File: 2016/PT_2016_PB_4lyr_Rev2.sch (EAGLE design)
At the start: 147 parts, among them M1+ ANDERSON_POWERPOLEPP45_PCB_HO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, M1- ANDERSON_POWERPOLEPP45_PCB_HO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, M2+ ANDERSON_POWERPOLEPP45_PCB_HO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, M2- ANDERSON_POWERPOLEPP45_PCB_HO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, M2-1 ANDERSON_POWERPOLEPP45_PCB_HO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, M2-2 ANDERSON_POWERPOLEPP45_PCB_HO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, M2-3 ANDERSON_POWERPOLEPP45_PCB_HO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, M2-4 ANDERSON_POWERPOLEPP45_PCB_HO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, M3+ ANDERSON_POWERPOLEPP45_PCB_HO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, M3- ANDERSON_POWERPOLEPP45_PCB_HO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, M4+ ANDERSON_POWERPOLEPP45_PCB_HO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, M4- ANDERSON_POWERPOLEPP45_PCB_HO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, M5+ ANDERSON_POWERPOLEPP45_PCB_HO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, M5- ANDERSON_POWERPOLEPP45_PCB_HO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, M6+ ANDERSON_POWERPOLEPP45_PCB_HO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, M6- ANDERSON_POWERPOLEPP45_PCB_HO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, Q1 Q_IRFS7437PbF, Q11 Q_IRFS7437PbF, Q12 2N7002, Q14 Q_IRFS7437PbF, Q16 Q_IRFS7437PbF, Q2 2N7002, Q20 Q_IRFS7437PbF, Q6 Q_IRFS7437PbF, Q7 Q_IRFS7437PbF, Q9 Q_IRFS7437PbF, X1 22-23-2041

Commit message: Added space for addition mounting wings and started moving components
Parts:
- removed M2-1, M2-2, M2-3, M2-4: ANDERSON_POWERPOLEPP45_PCB_HORIZ_RIGHT, MRDT-Connectors:ANDERSON_POWERPOLEPP45_PCB_HORIZ_RIGHT
- removed X1: 22-23-2041, con-molex:22-23-2041
- AUX1+, AUX2+, M1+, M2+, M3+, M4+, M5+, M6+: value ANDERSON_POWERPOLEPP45_PCB_HORIZ_RIGHT -> ANDERSON_POWERPOLEPP45_PCB_HORIZ_RIGHT_2HIGH; device MRDT-Connectors:ANDERSON_POWERPOLEPP45_PCB_HORIZ_RIGHT -> MRDT-Connectors:ANDERSON_POWERPOLEPP45_PCB_HORIZ_RIGHT_2HIGH
- C16, C24, C26, C28, C30, C32, C36, C7: value 10µF -> .1µF
- U$28, U$29: value ANDERSON_POWERPOLEPP45_PCB_HORIZ_RIGHT_2HIGH -> ANDERSON_POWERPOLEPP45_PCB_HORIZ_RIGHT; device MRDT-Connectors:ANDERSON_POWERPOLEPP45_PCB_HORIZ_RIGHT_2HIGH -> MRDT-Connectors:ANDERSON_POWERPOLEPP45_PCB_HORIZ_RIGHT
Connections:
- removed net N$11: M2-2.P$1, X1-1.S
- removed net N$3: M2-3.P$1, X1-4.S
- removed net N$5: M2-1.P$1, X1-3.S
- removed net N$8: M2-4.P$1, X1-2.S

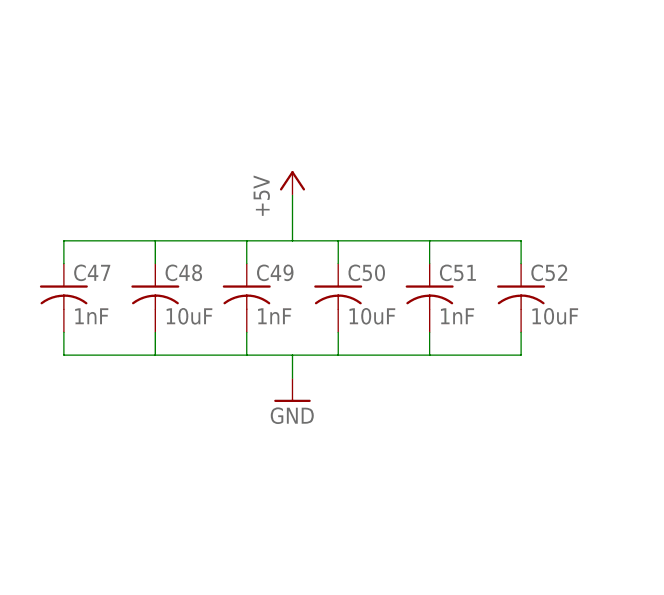
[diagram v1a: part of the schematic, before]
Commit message: Changed 5V Caps
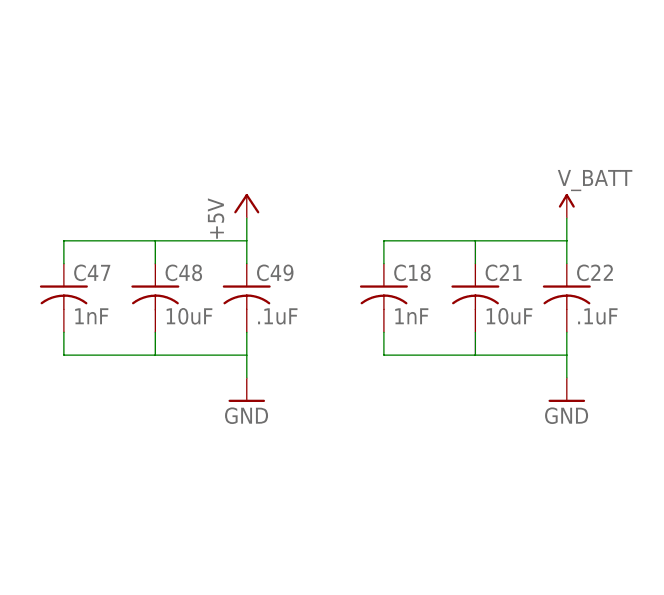
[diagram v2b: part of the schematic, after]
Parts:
- removed C50, C52: 10uF, resistor:C-USC1206
- removed C51: 1nF, resistor:C-USC1206
- added C18: 1nF, resistor:C-USC1206
- added C21: 10uF, resistor:C-USC1206
- added C22: .1uF, resistor:C-USC1206
- C49: value 1nF -> .1uF
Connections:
- net +5V: no longer C50.1, C51.1, C52.1
- net GND: now also C18.2, C21.2, C22.2; no longer C50.2, C51.2, C52.2
- net V_BATT: now also C18.1, C21.1, C22.1
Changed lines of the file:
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@@
 <part name="C47" library="resistor" deviceset="C-US" device="C1206" value="1nF"/>
 <part name="C48" library="resistor" deviceset="C-US" device="C1206" value="10uF"/>
-<part name="C49" library="resistor" deviceset="C-US" device="C1206" value="1nF"/>
-<part name="C50" library="resistor" deviceset="C-US" device="C1206" value="10uF"/>
-<part name="C51" library="resistor" deviceset="C-US" device="C1206" value="1nF"/>
-<part name="C52" library="resistor" deviceset="C-US" device="C1206" value="10uF"/>
+<part name="C49" library="resistor" deviceset="C-US" device="C1206" value=".1uF"/>
 <part name="P+25" library="supply1" deviceset="+5V" device=""/>
 <part name="GND95" library="SparkFun-Aesthetics" deviceset="GND" device=""/>
@@
 <part name="GND43" library="SparkFun-Aesthetics" deviceset="GND" device=""/>
 <part name="C17" library="resistor" deviceset="C-US" device="C1206" value="1nF"/>
+<part name="C18" library="resistor" deviceset="C-US" device="C1206" value="1nF"/>
+<part name="C21" library="resistor" deviceset="C-US" device="C1206" value="10uF"/>
+<part name="C22" library="resistor" deviceset="C-US" device="C1206" value=".1uF"/>
+<part name="GND45" library="SparkFun-Aesthetics" deviceset="GND" device=""/>
+<part name="SUPPLY16" library="SparkFun-Aesthetics" deviceset="V_BATT" device=""/>
 </parts>
 <sheets>
@@
 <instance part="GND94" gate="1" x="111.76" y="40.64"/>
 <instance part="C47" gate="G$1" x="195.58" y="5.08"/>
-<instance part="C48" gate="G$1" x="205.74" y="5.08"/>
-<instance part="C49" gate="G$1" x="215.9" y="5.08"/>
-<instance part="C50" gate="G$1" x="226.06" y="5.08"/>
-<instance part="C51" gate="G$1" x="236.22" y="5.08"/>
-<instance part="C52" gate="G$1" x="246.38" y="5.08"/>
-<instance part="P+25" gate="1" x="220.98" y="17.78"/>
-<instance part="GND95" gate="1" x="220.98" y="-7.62"/>
+<instance part="C48" gate="G$1" x="205.74" y="5.08" smashed="yes">
+<attribute name="NAME" x="206.756" y="5.715" size="1.778" layer="95"/>
+<attribute name="VALUE" x="206.756" y="0.889" size="1.778" layer="96"/>
+</instance>
+<instance part="C49" gate="G$1" x="215.9" y="5.08" smashed="yes">
+<attribute name="NAME" x="216.916" y="5.715" size="1.778" layer="95"/>
+<attribute name="VALUE" x="216.916" y="0.889" size="1.778" layer="96"/>
+</instance>
+<instance part="P+25" gate="1" x="215.9" y="15.24"/>
+<instance part="GND95" gate="1" x="215.9" y="-7.62"/>
 <instance part="SUPPLY2" gate="G$1" x="-518.16" y="231.14"/>
 <instance part="Q1" gate="G$1" x="-520.7" y="182.88"/>
@@
 <instance part="GND43" gate="1" x="73.66" y="114.3"/>
 <instance part="C17" gate="G$1" x="73.66" y="124.46"/>
+<instance part="C18" gate="G$1" x="231.14" y="5.08"/>
+<instance part="C21" gate="G$1" x="241.3" y="5.08" smashed="yes">
+<attribute name="NAME" x="242.316" y="5.715" size="1.778" layer="95"/>
+<attribute name="VALUE" x="242.316" y="0.889" size="1.778" layer="96"/>
+</instance>
+<instance part="C22" gate="G$1" x="251.46" y="5.08" smashed="yes">
+<attribute name="NAME" x="252.476" y="5.715" size="1.778" layer="95"/>
+<attribute name="VALUE" x="252.476" y="0.889" size="1.778" layer="96"/>
+</instance>
+<instance part="GND45" gate="1" x="251.46" y="-7.62"/>
+<instance part="SUPPLY16" gate="G$1" x="251.46" y="12.7"/>
 </instances>
 <busses>
@@
 <pinref part="C47" gate="G$1" pin="2"/>
 <wire x1="195.58" y1="0" x2="195.58" y2="-2.54" width="0.1524" layer="91"/>
-<pinref part="C52" gate="G$1" pin="2"/>
 <wire x1="195.58" y1="-2.54" x2="205.74" y2="-2.54" width="0.1524" layer="91"/>
-<wire x1="215.9" y1="-2.54" x2="220.98" y2="-2.54" width="0.1524" layer="91"/>
-<wire x1="220.98" y1="-2.54" x2="226.06" y2="-2.54" width="0.1524" layer="91"/>
-<wire x1="236.22" y1="-2.54" x2="246.38" y2="-2.54" width="0.1524" layer="91"/>
-<wire x1="246.38" y1="-2.54" x2="246.38" y2="0" width="0.1524" layer="91"/>
-<pinref part="C51" gate="G$1" pin="2"/>
-<wire x1="236.22" y1="0" x2="236.22" y2="-2.54" width="0.1524" layer="91"/>
-<pinref part="C50" gate="G$1" pin="2"/>
-<wire x1="236.22" y1="-2.54" x2="226.06" y2="-2.54" width="0.1524" layer="91"/>
-<wire x1="226.06" y1="-2.54" x2="226.06" y2="0" width="0.1524" layer="91"/>
 <pinref part="C49" gate="G$1" pin="2"/>
 <wire x1="215.9" y1="0" x2="215.9" y2="-2.54" width="0.1524" layer="91"/>
@@
 <wire x1="205.74" y1="-2.54" x2="205.74" y2="0" width="0.1524" layer="91"/>
 <pinref part="GND95" gate="1" pin="GND"/>
-<wire x1="220.98" y1="-5.08" x2="220.98" y2="-2.54" width="0.1524" layer="91"/>
+<wire x1="215.9" y1="-5.08" x2="215.9" y2="-2.54" width="0.1524" layer="91"/>
 </segment>
 <segment>
@@
 <pinref part="GND43" gate="1" pin="GND"/>
 <wire x1="73.66" y1="119.38" x2="73.66" y2="116.84" width="0.1524" layer="91"/>
+</segment>
+<segment>
+<pinref part="C18" gate="G$1" pin="2"/>
+<wire x1="231.14" y1="0" x2="231.14" y2="-2.54" width="0.1524" layer="91"/>
+<wire x1="231.14" y1="-2.54" x2="241.3" y2="-2.54" width="0.1524" layer="91"/>
+<pinref part="C22" gate="G$1" pin="2"/>
+<wire x1="251.46" y1="0" x2="251.46" y2="-2.54" width="0.1524" layer="91"/>
+<pinref part="C21" gate="G$1" pin="2"/>
+<wire x1="251.46" y1="-2.54" x2="241.3" y2="-2.54" width="0.1524" layer="91"/>
+<wire x1="241.3" y1="-2.54" x2="241.3" y2="0" width="0.1524" layer="91"/>
+<pinref part="GND45" gate="1" pin="GND"/>
+<wire x1="251.46" y1="-5.08" x2="251.46" y2="-2.54" width="0.1524" layer="91"/>
 </segment>
 </net>
@@
 <wire x1="-68.58" y1="-38.1" x2="-55.88" y2="-38.1" width="0.1524" layer="91"/>
 </segment>
+<segment>
+<pinref part="C18" gate="G$1" pin="1"/>
+<wire x1="231.14" y1="7.62" x2="231.14" y2="10.16" width="0.1524" layer="91"/>
+<wire x1="231.14" y1="10.16" x2="241.3" y2="10.16" width="0.1524" layer="91"/>
+<wire x1="251.46" y1="12.7" x2="251.46" y2="10.16" width="0.1524" layer="91"/>
+<pinref part="C22" gate="G$1" pin="1"/>
+<wire x1="251.46" y1="7.62" x2="251.46" y2="10.16" width="0.1524" layer="91"/>
+<pinref part="C21" gate="G$1" pin="1"/>
+<wire x1="251.46" y1="10.16" x2="241.3" y2="10.16" width="0.1524" layer="91"/>
+<wire x1="241.3" y1="10.16" x2="241.3" y2="7.62" width="0.1524" layer="91"/>
+<pinref part="SUPPLY16" gate="G$1" pin="V_BATT"/>
+</segment>
 </net>
 <net name="+5V" class="0">
@@
 <pinref part="P+25" gate="1" pin="+5V"/>
 <wire x1="195.58" y1="10.16" x2="205.74" y2="10.16" width="0.1524" layer="91"/>
-<wire x1="220.98" y1="15.24" x2="220.98" y2="10.16" width="0.1524" layer="91"/>
-<pinref part="C52" gate="G$1" pin="1"/>
-<wire x1="220.98" y1="10.16" x2="226.06" y2="10.16" width="0.1524" layer="91"/>
-<wire x1="226.06" y1="10.16" x2="236.22" y2="10.16" width="0.1524" layer="91"/>
-<wire x1="236.22" y1="10.16" x2="246.38" y2="10.16" width="0.1524" layer="91"/>
-<wire x1="246.38" y1="10.16" x2="246.38" y2="7.62" width="0.1524" layer="91"/>
-<pinref part="C51" gate="G$1" pin="1"/>
-<wire x1="236.22" y1="7.62" x2="236.22" y2="10.16" width="0.1524" layer="91"/>
-<pinref part="C50" gate="G$1" pin="1"/>
-<wire x1="226.06" y1="7.62" x2="226.06" y2="10.16" width="0.1524" layer="91"/>
+<wire x1="215.9" y1="12.7" x2="215.9" y2="10.16" width="0.1524" layer="91"/>
 <pinref part="C49" gate="G$1" pin="1"/>
-<wire x1="220.98" y1="10.16" x2="215.9" y2="10.16" width="0.1524" layer="91"/>
 <wire x1="215.9" y1="7.62" x2="215.9" y2="10.16" width="0.1524" layer="91"/>
 <pinref part="C48" gate="G$1" pin="1"/>

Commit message: rerouting...
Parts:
- removed C10: 1uF, resistor:C-USC1206
- added C34, C44, C50, C51, C52, C53: 1uF, resistor:C-USC1206
- added U$30, U$31, U$32, U$33, U$34, U$35: APP_MOUTING_WINGHORIZ, MRDT-Connectors:APP_MOUTING_WINGHORIZ
- C13, C14, C15, C17: value 1nF -> 1uF
- U$2: device MRDT-2015-PowerBoard:Q_ACS714_SKETCH -> MRDT-2015-PowerBoard:Q_ACS714
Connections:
- new net N$11: C51.1
- new net N$3: C34.1
- new net N$5: C44.1
- new net N$71: C52.1
- new net N$72: C53.1
- new net N$8: C50.1
- net +5V: no longer C10.1
- net AUX_P-SIG: now also U$4.PA7; no longer U$4.PQ1
- net AUX_P2-SIG: now also U$4.PP5; no longer U$4.PK7
- net GND: now also C34.2, C44.2, C50.2, C51.2, C52.2, C53.2; no longer C10.2
- net M1-SIG: now also U$4.PK7; no longer U$4.PP5
- net M2-SIG: now also U$4.PQ1; no longer U$4.PA7
- net M3-SIG: now also U$4.PK6; no longer U$4.PH0
- net M4-SIG: now also U$4.PP3; no longer U$4.PH1
- net M5-SIG: now also U$4.PH1; no longer U$4.PP3
- net M6-SIG: now also U$4.PH0; no longer U$4.PK6
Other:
- moved on the sheet: AUX1+, AUX1-, AUX2+, AUX2-, C13, C14, C15, C17, C19, C20, C45, C46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

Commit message: Routing
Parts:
- removed AUX1+, AUX2+, M1+, M2+, M3+, M4+, M5+, M6+: ANDERSON_POWERPOLEPP45_PCB_HORIZ_RIGHT_2HIGH, MRDT-Connectors:ANDERSON_POWERPOLEPP45_PCB_HORIZ_RIGHT_2HIGH
- removed AUX1-, AUX2-, M1-, M2-, M3-, M4-, M5-, M6-: ANDERSON_POWERPOLEPP45_PCB_HORIZ_RIGHT, MRDT-Connectors:ANDERSON_POWERPOLEPP45_PCB_HORIZ_RIGHT
- removed C16, C23, C24, C25, C26, C28, C29, C30, C32, C33, C36, C39, C41, C5, C7, C8: .1µF, resistor:C-USC1206
- removed C27, C31, C35, C37, C38, C40, C42, C9: 1nF, resistor:C-USC1206
- removed LED1, LED10, LED11, LED12, LED6, LED7, LED8, LED9: (no value), SparkFun-LED:LED1206
- removed Q1, Q11, Q14, Q16, Q20, Q6, Q7, Q9: Q_IRFS7437PbF, MRDT-2015-PowerBoard:Q_IRF7437SMD
- removed R16, R18, R20, R22, R24, R28, R5, R9: 5kΩ, SparkFun-Passives:RESISTOR1206
- removed U$10, U$11, U$13, U$6, U$7, U$8, U$9: LT1910, Jake:LT1910
- removed U$14, U$15, U$16, U$17, U$18, U$19, U$20: ACS714LLCTR-50A-T, MRDT-2015-PowerBoard:Q_ACS714_SKETCH
- added ACS714-M1, ACS714-M2, ACS714-M3, ACS714-M4, ACS714-M5, ACS714-M6, ACS714-M7, ACS714-M8: ACS714LLCTR-50A-T, MRDT-2015-PowerBoard:Q_ACS714
- added ACS714CAP-M1, ACS714CAP-M2, ACS714CAP-M3, ACS714CAP-M4, ACS714CAP-M5, ACS714CAP-M6, ACS714CAP-M7, ACS714CAP-M8, LT1910CAP-M1, LT1910CAP-M2, LT1910CAP-M3, LT1910CAP-M4, LT1910CAP-M5, LT1910CAP-M6, LT1910CAP-M7, LT1910CAP-M8: .1µF, resistor:C-USC1206
- added BOTAPP-M1, BOTAPP-M2, BOTAPP-M3, BOTAPP-M4, BOTAPP-M5, BOTAPP-M6, BOTAPP-M7, BOTAPP-M8: ANDERSON_POWERPOLEPP45_PCB_HORIZ_RIGHT, MRDT-Connectors:ANDERSON_POWERPOLEPP45_PCB_HORIZ_RIGHT
- added FET-M1, FET-M2, FET-M3, FET-M4, FET-M5, FET-M6, FET-M7, FET-M8: Q_IRFS7437PbF, MRDT-2015-PowerBoard:Q_IRF7437SMD
- added FILTERCAP-M1, FILTERCAP-M2, FILTERCAP-M3, FILTERCAP-M4, FILTERCAP-M5, FILTERCAP-M6, FILTERCAP-M7, FILTERCAP-M8: 1nF, resistor:C-USC1206
- added LED-M1, LED-M2, LED-M3, LED-M4, LED-M5, LED-M6, LED-M7, LED-M8: (no value), SparkFun-LED:LED1206
- added LEDRES-M1, LEDRES-M2, LEDRES-M3, LEDRES-M4, LEDRES-M5, LEDRES-M6, LEDRES-M7, LEDRES-M8: 5kΩ, SparkFun-Passives:RESISTOR1206
- added LT1910-M1, LT1910-M2, LT1910-M3, LT1910-M4, LT1910-M5, LT1910-M6, LT1910-M7, LT1910-M8: LT1910, Jake:LT1910
- added TOPAPP-M1, TOPAPP-M2, TOPAPP-M3, TOPAPP-M4, TOPAPP-M5, TOPAPP-M6, TOPAPP-M7, TOPAPP-M8: ANDERSON_POWERPOLEPP45_PCB_HORIZ_RIGHT_2HIGH, MRDT-Connectors:ANDERSON_POWERPOLEPP45_PCB_HORIZ_RIGHT_2HIGH
- U$1: value LT1910 -> TIVA-C-CONNECTED; device Jake:LT1910 -> MRDT-2015-General:TIVA-C-CONNECTED
- U$2: value ACS714LLCTR-50A-T -> APP_MOUTING_WINGHORIZ; device MRDT-2015-PowerBoard:Q_ACS714 -> MRDT-Connectors:APP_MOUTING_WINGHORIZ
- U$4: value TIVA-C-CONNECTED -> APP_MOUTING_WINGHORIZ; device MRDT-2015-General:TIVA-C-CONNECTED -> MRDT-Connectors:APP_MOUTING_WINGHORIZ
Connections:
- removed net AUX_P-IMEAS: U$20.VIOUT, U$4.PB4
- removed net AUX_P-SIG: U$13.IN, U$4.PA7
- removed net AUX_P2-IMEAS: U$2.VIOUT, U$4.PD2
- removed net AUX_P2-SIG: U$1.IN, U$4.PP5
- removed net M1-IMEAS: U$14.VIOUT, U$4.PK3
- removed net M1-SIG: U$4.PK7, U$6.IN
- removed net M2-IMEAS: U$15.VIOUT, U$4.PK2
- removed net M2-SIG: U$4.PQ1, U$7.IN
- removed net M3-IMEAS: U$19.VIOUT, U$4.PK1
- removed net M3-SIG: U$4.PK6, U$8.IN
- removed net M4-IMEAS: U$18.VIOUT, U$4.PD4
- removed net M4-SIG: U$4.PP3, U$9.IN
- removed net M5-IMEAS: U$17.VIOUT, U$4.PK0
- removed net M5-SIG: U$10.IN, U$4.PH1
- removed net M6-IMEAS: U$16.VIOUT, U$4.PB5
- removed net M6-SIG: U$11.IN, U$4.PH0
- removed net N$1: C37.1, U$14.FILTER
- removed net N$10: AUX2+.P$1, Q1.S, R5.1
- removed net N$11: C51.1
- removed net N$14: Q1.G, U$1.GATE
- removed net N$15: LED11.A, R5.2
- removed net N$16: C9.1, U$2.FILTER
- removed net N$17: C27.1, U$16.FILTER
- removed net N$18: C14.1
- removed net N$19: C15.1
- removed net N$2: C38.1, U$15.FILTER
- removed net N$20: C17.1
- removed net N$22: C31.1, U$17.FILTER
- removed net N$23: C35.1, U$18.FILTER
- removed net N$24: C40.1, U$19.FILTER
- removed net N$25: C42.1, U$20.FILTER
- removed net N$28: C24.2, Q7.D, U$15.IP-, U$7.SENSE, U$7.V+
- removed net N$29: M2+.P$1, Q7.S, R16.1
- removed net N$3: C34.1
- removed net N$30: Q7.G, U$7.GATE
- removed net N$31: LED6.A, R16.2
- removed net N$39: LED1.A, R9.2
- removed net N$40: C16.2, Q6.D, U$14.IP-, U$6.SENSE, U$6.V+
- removed net N$41: M1+.P$1, Q6.S, R9.1
- removed net N$42: Q6.G, U$6.GATE
- removed net N$44: C26.2, Q9.D, U$19.IP-, U$8.SENSE, U$8.V+
- removed net N$45: M3+.P$1, Q9.S, R18.1
- removed net N$47: Q9.G, U$8.GATE
- removed net N$49: LED7.A, R18.2
- removed net N$5: C44.1
- removed net N$54: C28.2, Q11.D, U$18.IP-, U$9.SENSE, U$9.V+
- removed net N$55: M4+.P$1, Q11.S, R20.1
- removed net N$56: Q11.G, U$9.GATE
- removed net N$57: LED8.A, R20.2
- removed net N$60: C30.2, Q14.D, U$10.SENSE, U$10.V+, U$17.IP-
- removed net N$61: M5+.P$1, Q14.S, R22.1
- removed net N$62: Q14.G, U$10.GATE
- removed net N$63: LED9.A, R22.2
- removed net N$66: C32.2, Q16.D, U$11.SENSE, U$11.V+, U$16.IP-
- removed net N$67: M6+.P$1, Q16.S, R24.1
- removed net N$68: Q16.G, U$11.GATE
- removed net N$69: LED10.A, R24.2
- removed net N$7: C13.1, REY-5V.+SENSE, REY-5V.+VOUT, U$3.IP+
- removed net N$72: C53.1
- removed net N$78: C36.2, Q20.D, U$13.SENSE, U$13.V+, U$20.IP-
- removed net N$79: AUX1+.P$1, Q20.S, R28.1
- removed net N$8: C50.1
- removed net N$80: Q20.G, U$13.GATE
- removed net N$81: LED12.A, R28.2
- removed net N$9: C7.2, Q1.D, U$1.SENSE, U$1.V+, U$2.IP-
- new net DRAIN-M1: ACS714-M1.IP-, FET-M1.D, LT1910-M1.SENSE, LT1910-M1.V+, LT1910CAP-M1.2
- new net DRAIN-M2: ACS714-M2.IP-, FET-M2.D, LT1910-M2.SENSE, LT1910-M2.V+, LT1910CAP-M2.2
- new net DRAIN-M3: ACS714-M3.IP-, FET-M3.D, LT1910-M3.SENSE, LT1910-M3.V+, LT1910CAP-M3.2
- new net DRAIN-M4: ACS714-M4.IP-, FET-M4.D, LT1910-M4.SENSE, LT1910-M4.V+, LT1910CAP-M4.2
- new net DRAIN-M5: ACS714-M5.IP-, FET-M5.D, LT1910-M5.SENSE, LT1910-M5.V+, LT1910CAP-M5.2
- new net DRAIN-M6: ACS714-M6.IP-, FET-M6.D, LT1910-M6.SENSE, LT1910-M6.V+, LT1910CAP-M6.2
- new net DRAIN-M7: ACS714-M7.IP-, FET-M7.D, LT1910-M7.SENSE, LT1910-M7.V+, LT1910CAP-M7.2
- new net DRAIN-M8: ACS714-M8.IP-, FET-M8.D, LT1910-M8.SENSE, LT1910-M8.V+, LT1910CAP-M8.2
- new net FILTER-M1: ACS714-M1.FILTER, FILTERCAP-M1.1
- new net FILTER-M2: ACS714-M2.FILTER, FILTERCAP-M2.1
- new net FILTER-M3: ACS714-M3.FILTER, FILTERCAP-M3.1
- new net FILTER-M4: ACS714-M4.FILTER, FILTERCAP-M4.1
- new net FILTER-M5: ACS714-M5.FILTER, FILTERCAP-M5.1
- new net FILTER-M6: ACS714-M6.FILTER, FILTERCAP-M6.1
- new net FILTER-M7: ACS714-M7.FILTER, FILTERCAP-M7.1
- new net FILTER-M8: ACS714-M8.FILTER, FILTERCAP-M8.1
- new net GATE-M1: FET-M1.G, LT1910-M1.GATE
- new net GATE-M2: FET-M2.G, LT1910-M2.GATE
- new net GATE-M3: FET-M3.G, LT1910-M3.GATE
- new net GATE-M4: FET-M4.G, LT1910-M4.GATE
- new net GATE-M5: FET-M5.G, LT1910-M5.GATE
- new net GATE-M6: FET-M6.G, LT1910-M6.GATE
- new net GATE-M7: FET-M7.G, LT1910-M7.GATE
- new net GATE-M8: FET-M8.G, LT1910-M8.GATE
- new net IMEAS-M1: ACS714-M1.VIOUT, U$1.PK3
- new net IMEAS-M2: ACS714-M2.VIOUT, U$1.PK2
- new net IMEAS-M3: ACS714-M3.VIOUT, U$1.PK1
- new net IMEAS-M4: ACS714-M4.VIOUT, U$1.PD4
- new net IMEAS-M5: ACS714-M5.VIOUT, U$1.PK0
- new net IMEAS-M6: ACS714-M6.VIOUT, U$1.PB5
- new net IMEAS-M7: ACS714-M7.VIOUT, U$1.PB4
- new net IMEAS-M8: ACS714-M8.VIOUT, U$1.PD2
- new net LEDLINE-M1: LED-M1.A, LEDRES-M1.2
- new net LEDLINE-M2: LED-M2.A, LEDRES-M2.2
- new net LEDLINE-M3: LED-M3.A, LEDRES-M3.2
- new net LEDLINE-M4: LED-M4.A, LEDRES-M4.2
- new net LEDLINE-M5: LED-M5.A, LEDRES-M5.2
- new net LEDLINE-M6: LED-M6.A, LEDRES-M6.2
- new net LEDLINE-M7: LED-M7.A, LEDRES-M7.2
- new net LEDLINE-M8: LED-M8.A, LEDRES-M8.2
- new net SIG-M1: LT1910-M1.IN, U$1.PK7
- new net SIG-M2: LT1910-M2.IN, U$1.PQ1
- new net SIG-M3: LT1910-M3.IN, U$1.PK6
- new net SIG-M4: LT1910-M4.IN, U$1.PP3
- new net SIG-M5: LT1910-M5.IN, U$1.PH1
- new net SIG-M6: LT1910-M6.IN, U$1.PH0
- new net SIG-M7: LT1910-M7.IN, U$1.PA7
- new net SIG-M8: LT1910-M8.IN, U$1.PP5
- new net SOURCE-M1: FET-M1.S, LEDRES-M1.1, TOPAPP-M1.P$1
- new net SOURCE-M2: FET-M2.S, LEDRES-M2.1, TOPAPP-M2.P$1
- new net SOURCE-M3: FET-M3.S, LEDRES-M3.1, TOPAPP-M3.P$1
- new net SOURCE-M4: FET-M4.S, LEDRES-M4.1, TOPAPP-M4.P$1
- new net SOURCE-M5: FET-M5.S, LEDRES-M5.1, TOPAPP-M5.P$1
- new net SOURCE-M6: FET-M6.S, LEDRES-M6.1, TOPAPP-M6.P$1
- new net SOURCE-M7: FET-M7.S, LEDRES-M7.1, TOPAPP-M7.P$1
- new net SOURCE-M8: FET-M8.S, LEDRES-M8.1, TOPAPP-M8.P$1
- net +5V: now also ACS714-M1.VCC, ACS714-M2.VCC, ACS714-M3.VCC, ACS714-M4.VCC, ACS714-M5.VCC, ACS714-M6.VCC, ACS714-M7.VCC, ACS714-M8.VCC, ACS714CAP-M1.2, ACS714CAP-M2.2, ACS714CAP-M3.2, ACS714CAP-M4.2, ACS714CAP-M5.2, ACS714CAP-M6.2, ACS714CAP-M7.2, ACS714CAP-M8.2, U$1.+5V; no longer C23.2, C25.2, C29.2, C33.2, C39.2, C41.2, C5.2, C8.2, U$14.VCC, U$15.VCC, U$16.VCC, U$17.VCC, U$18.VCC, U$19.VCC, U$2.VCC, U$20.VCC, U$4.+5V
- net 12V-IMEAS: now also U$1.PD1; no longer U$4.PD1
- net 12V-SIG: now also U$1.PN3; no longer U$4.PN3
- net 5V-IMEAS: now also U$1.PD0; no longer U$4.PD0
- net 5V-SIG: now also U$1.PP2; no longer U$4.PP2
- net GND: now also ACS714-M1.GND, ACS714-M2.GND, ACS714-M3.GND, ACS714-M4.GND, ACS714-M5.GND, ACS714-M6.GND, ACS714-M7.GND, ACS714-M8.GND, ACS714CAP-M1.1, ACS714CAP-M2.1, ACS714CAP-M3.1, ACS714CAP-M4.1, ACS714CAP-M5.1, ACS714CAP-M6.1, ACS714CAP-M7.1, ACS714CAP-M8.1, BOTAPP-M1.P$1, BOTAPP-M2.P$1, BOTAPP-M3.P$1, BOTAPP-M4.P$1, BOTAPP-M5.P$1, BOTAPP-M6.P$1, BOTAPP-M7.P$1, BOTAPP-M8.P$1, FILTERCAP-M1.2, FILTERCAP-M2.2, FILTERCAP-M3.2, FILTERCAP-M4.2, FILTERCAP-M5.2, FILTERCAP-M6.2, FILTERCAP-M7.2, FILTERCAP-M8.2, LED-M1.C, LED-M2.C, LED-M3.C, LED-M4.C, LED-M5.C, LED-M6.C, LED-M7.C, LED-M8.C, LT1910-M1.GND, LT1910-M2.GND, LT1910-M3.GND, LT1910-M4.GND, LT1910-M5.GND, LT1910-M6.GND, LT1910-M7.GND, LT1910-M8.GND, LT1910CAP-M1.1, LT1910CAP-M2.1, LT1910CAP-M3.1, LT1910CAP-M4.1, LT1910CAP-M5.1, LT1910CAP-M6.1, LT1910CAP-M7.1, LT1910CAP-M8.1; no longer AUX1-.P$1, AUX2-.P$1, C16.1, C23.1, C24.1, C25.1, C26.1, C27.2, C28.1, C29.1, C30.1, C31.2, C32.1, C33.1, C35.2, C36.1, C37.2, C38.2, C39.1, C40.2, C41.1, C42.2, C5.1, C7.1, C8.1, C9.2, LED1.C, LED10.C, LED11.C, LED12.C, LED6.C, LED7.C, LED8.C, LED9.C, M1-.P$1, M2-.P$1, M3-.P$1, M4-.P$1, M5-.P$1, M6-.P$1, U$10.GND, U$11.GND, U$13.GND, U$14.GND, U$15.GND, U$16.GND, U$17.GND, U$18.GND, U$19.GND, U$2.GND, U$20.GND, U$4.GND, U$6.GND, U$7.GND, U$8.GND, U$9.GND
- net N$100: now also U$1.RST; no longer U$4.RST
- net N$101: now also U$1.PB2; no longer U$4.PB2
- net N$102: now also U$1.PB3; no longer U$4.PB3
- net N$108: now also U$1.PD3; no longer U$4.PD3
- net N$110: now also U$1.PD5; no longer U$4.PD5
- net N$112: now also U$1.PE0; no longer U$4.PE0
- net N$113: now also U$1.PE1; no longer U$4.PE1
- net N$115: now also U$1.PE2; no longer U$4.PE2
- net N$116: now also U$1.PE3; no longer U$4.PE3
- net N$117: now also U$1.PE4; no longer U$4.PE4
- net N$118: now also U$1.PE5; no longer U$4.PE5
- net N$119: now also U$1.PG0; no longer U$4.PG0
- net N$120: now also U$1.PG1; no longer U$4.PG1
- net N$121: now also U$1.PL0; no longer U$4.PL0
- net N$122: now also U$1.PL1; no longer U$4.PL1
- net N$123: now also U$1.PL2; no longer U$4.PL2
- net N$124: now also U$1.PL3; no longer U$4.PL3
- net N$125: now also U$1.PL4; no longer U$4.PL4
- net N$129: now also U$1.PN4; no longer U$4.PN4
- net N$130: now also U$1.PN5; no longer U$4.PN5
- net N$131: now also U$1.PQ0; no longer U$4.PQ0
- net N$133: now also U$1.PQ2/PA3; no longer U$4.PQ2/PA3
- net N$134: now also U$1.PQ3/PA2; no longer U$4.PQ3/PA2
- net N$21: now also U$1.PH3; no longer U$4.PH3
- net N$35: now also U$1.PA4; no longer U$4.PA4
- net N$36: now also U$1.PA5; no longer U$4.PA5
- net N$37: now also U$1.PA6; no longer U$4.PA6
- net N$50: now also U$1.PC6; no longer U$4.PC6
- net N$51: now also U$1.PC7; no longer U$4.PC7
- net N$52: now also U$1.PF1; no longer U$4.PF1
- net N$53: now also U$1.PF2; no longer U$4.PF2
- net N$58: now also U$1.PF3; no longer U$4.PF3
- net N$70: now also U$1.PH2; no longer U$4.PH2
- net N$71: now also C13.1, C14.1, C15.1, C17.1, C34.1, C44.1, C50.1, C51.1, C53.1, REY-5V.+SENSE, REY-5V.+VOUT, U$3.IP+
- net N$75: now also U$1.PK4; no longer U$4.PK4
- net N$82: now also U$1.PK5; no longer U$4.PK5
- net N$83: now also U$1.PM0; no longer U$4.PM0
- net N$84: now also U$1.PM1; no longer U$4.PM1
- net N$85: now also U$1.PM2; no longer U$4.PM2
- net N$86: now also U$1.PM3; no longer U$4.PM3
- net N$87: now also U$1.PM4; no longer U$4.PM4
- net N$88: now also U$1.PM5; no longer U$4.PM5
- net N$89: now also U$1.PM6; no longer U$4.PM6
- net N$90: now also U$1.PM7; no longer U$4.PM7
- net N$93: now also U$1.PP4; no longer U$4.PP4
- net N$96: now also U$1.PN2; no longer U$4.PN2
- net N$98: now also U$1.+3V3; no longer U$4.+3V3
- net N$99: now also U$1.PL5; no longer U$4.PL5
- net PRIMARY-VMEAS: now also U$1.PD7; no longer U$4.PD7
- net RX1: now also U$1.PC4; no longer U$4.PC4
- net RX2: now also U$1.PP0; no longer U$4.PP0
- net TX1: now also U$1.PC5; no longer U$4.PC5
- net TX2: now also U$1.PP1; no longer U$4.PP1
- net V_BATT: now also ACS714-M1.IP+, ACS714-M2.IP+, ACS714-M3.IP+, ACS714-M4.IP+, ACS714-M5.IP+, ACS714-M6.IP+, ACS714-M7.IP+, ACS714-M8.IP+; no longer U$14.IP+, U$15.IP+, U$16.IP+, U$17.IP+, U$18.IP+, U$19.IP+, U$2.IP+, U$20.IP+

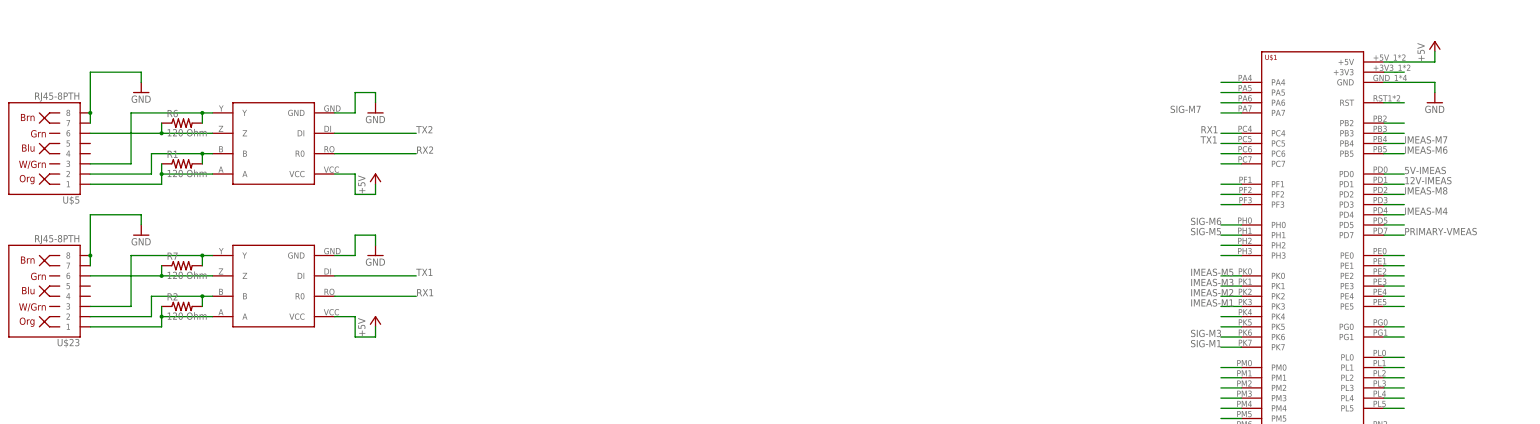
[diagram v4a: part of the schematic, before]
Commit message: Finished routing 4-layer
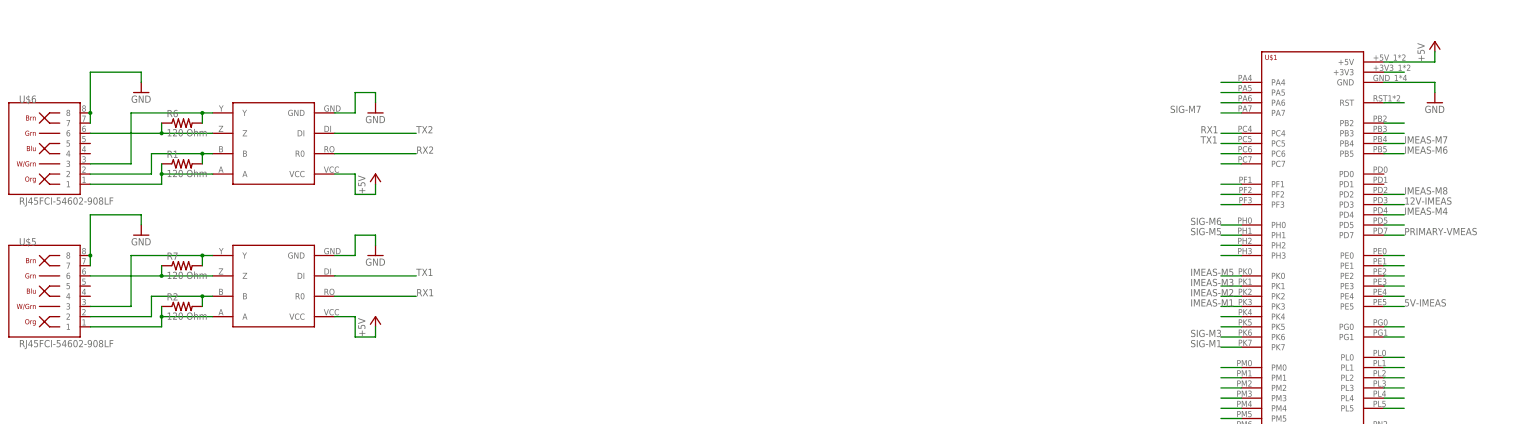
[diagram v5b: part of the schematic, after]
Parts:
- removed U$23: RJ45-8PTH, SparkFun-Connectors:RJ45-8PTH
- added U$6: RJ45FCI-54602-908LF, MRDT-2015-General:RJ45FCI-54602-908LF
- U$5: value RJ45-8PTH -> RJ45FCI-54602-908LF; device SparkFun-Connectors:RJ45-8PTH -> MRDT-2015-General:RJ45FCI-54602-908LF
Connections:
- removed net N$108: U$1.PD3
- removed net N$118: U$1.PE5
- net 12V-IMEAS: now also U$1.PD3; no longer U$1.PD1
- net 5V-IMEAS: now also U$1.PE5; no longer U$1.PD0
- net GND: now also U$6.7, U$6.8; no longer U$23.7, U$23.8
- net REC+: now also U$6.1; no longer U$5.1
- net REC+1: now also U$5.1; no longer U$23.1
- net REC-: now also U$6.2; no longer U$5.2
- net REC-1: now also U$5.2; no longer U$23.2
- net TRANS+: now also U$6.3; no longer U$5.3
- net TRANS+1: now also U$5.3; no longer U$23.3
- net TRANS-: now also U$6.6; no longer U$5.6
- net TRANS-1: now also U$5.6; no longer U$23.6
